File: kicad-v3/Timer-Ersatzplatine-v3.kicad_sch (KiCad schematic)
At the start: 16 parts, among them J1 250-204, J4 OLED SSD1306 0,91 Zoll, K1 G3VM-601AY2, SW1 Taster T1, SW2 Taster T2, SW3 Taster T3, U1 ESP32-C3 Super Mini, X1 250-202, X2 Last, X3 Snubber

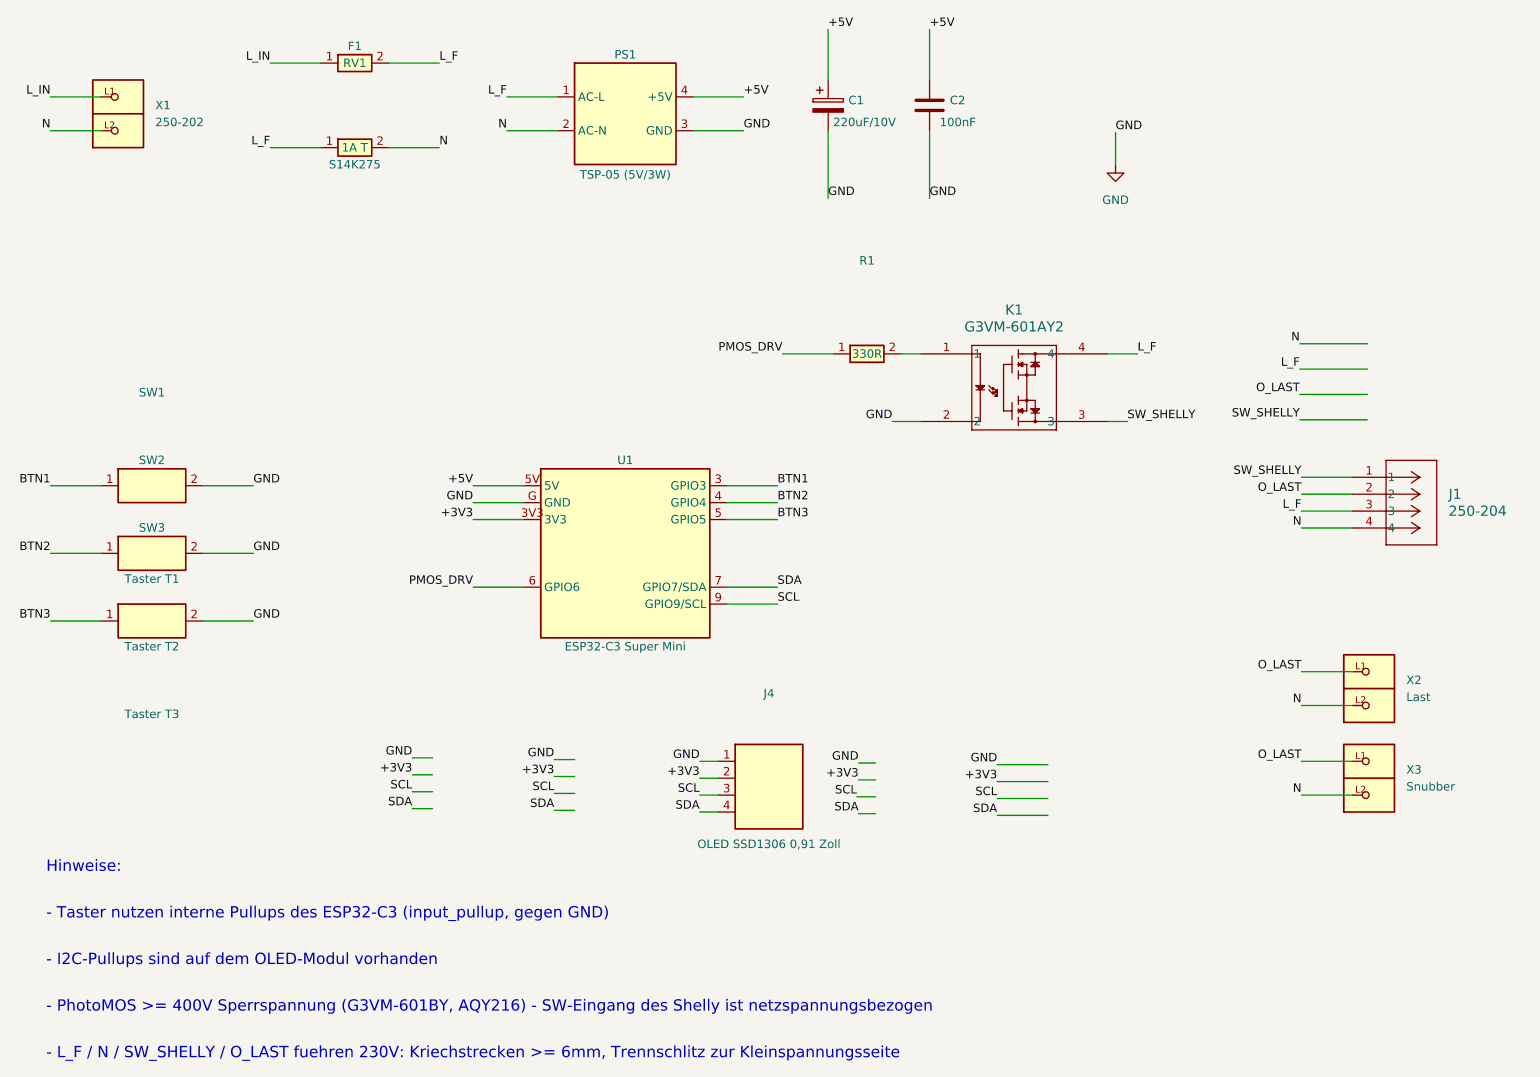
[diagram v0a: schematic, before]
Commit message: v3.0.1: K1 3/4-Tausch, 230V auf Innenlagen, J4-Drehung (GND unten)
Aufbauend auf v3.0.0 (Re-Layout + Umbenennung), Board-Feinschliff:
- K1 (PhotoMOS) Pin 3/4 getauscht (Schaltplan + Board) -> L_F via-los geroutet
- Alle 230V-Bahnen auf Innenlagen verschoben: F.Cu->In1, B.Cu->In2
  (Aussenflaechen 230V-frei/beruehrsicher; GND-Zonen identisch, DRC sauber)
- J4 (OLED-Header) um 180 Grad gedreht: GND jetzt unten zu PS1;
  Reihenfolge GND/VCC/SCL/SDA, neu geroutet, GND-Zone um J4.1 ergaenzt
- Schwachstrom-Bahnen + Silk (Nutzer-GUI) nachgezogen
- DRC: 0 unverbunden, 0 Clearance/Kriechstrecke/Short (nur kosmetische Silk)
- FW_VERSION 3.0.0 -> 3.0.1; firmware/build/ neu kompiliert

Finale GUI-DRC-Kriechstreckenpruefung (K1-Waiver) durch Nutzer erfolgt.

Co-Authored-By: Claude Opus 4.8 <noreply@anthropic.com>
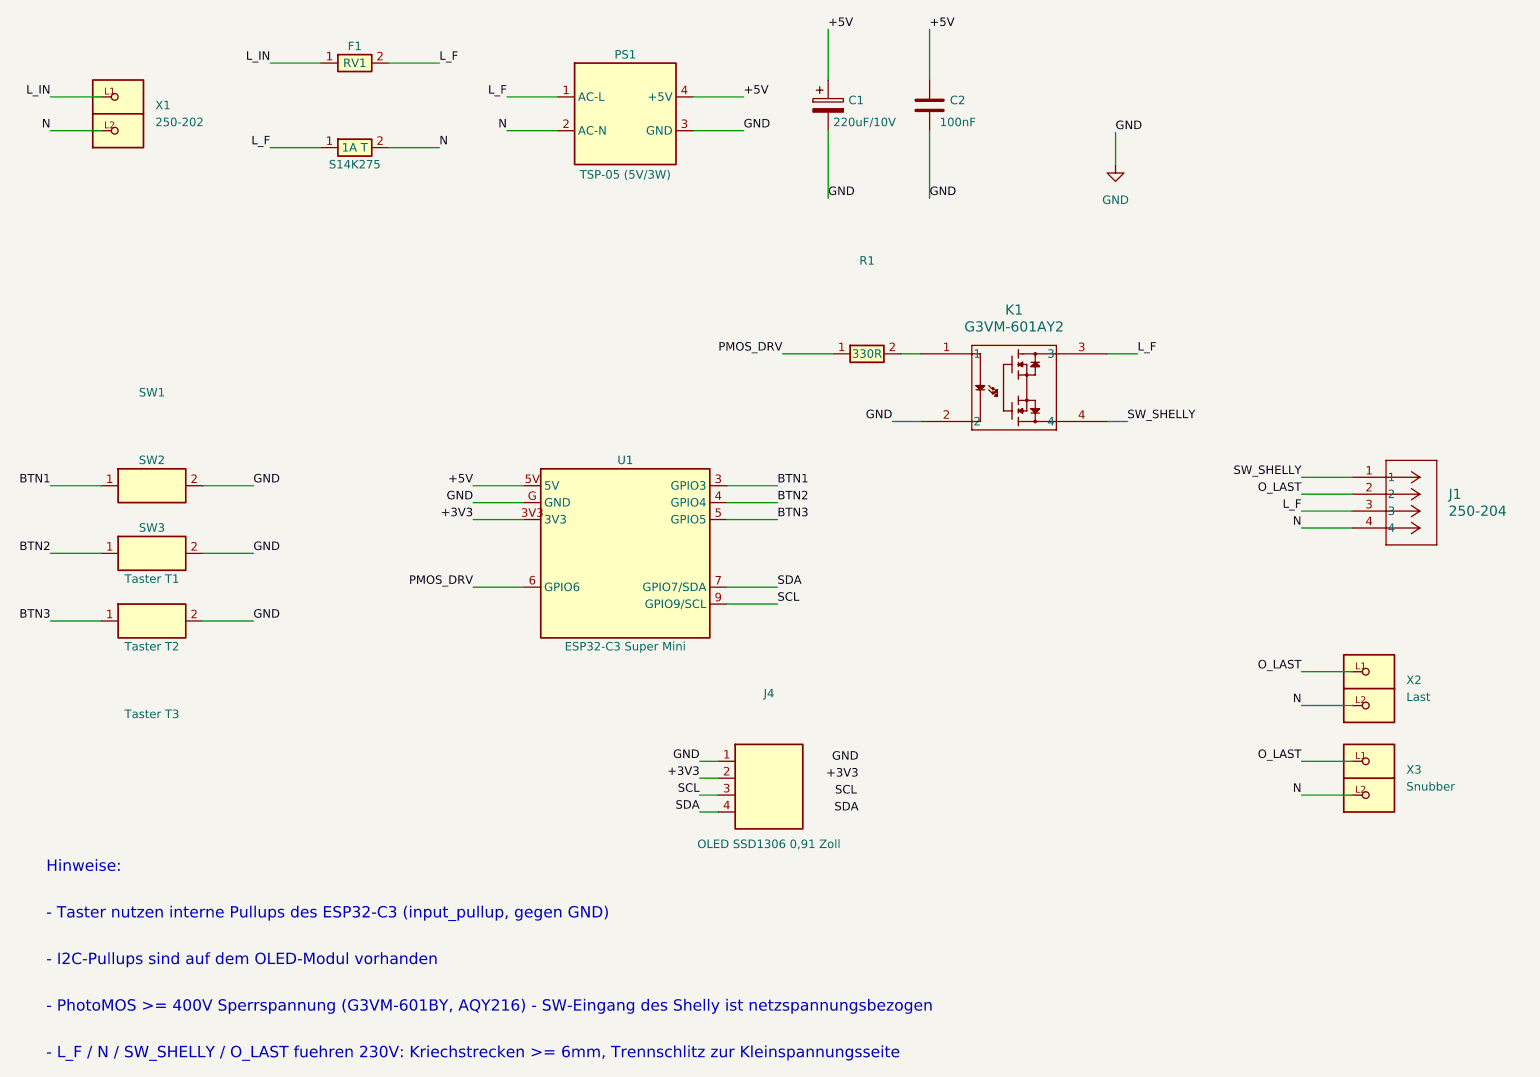
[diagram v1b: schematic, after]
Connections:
- net L_F: now also K1.3; no longer K1.4
- net SW_SHELLY: now also K1.4; no longer K1.3
